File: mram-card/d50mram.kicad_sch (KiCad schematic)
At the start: 42 parts

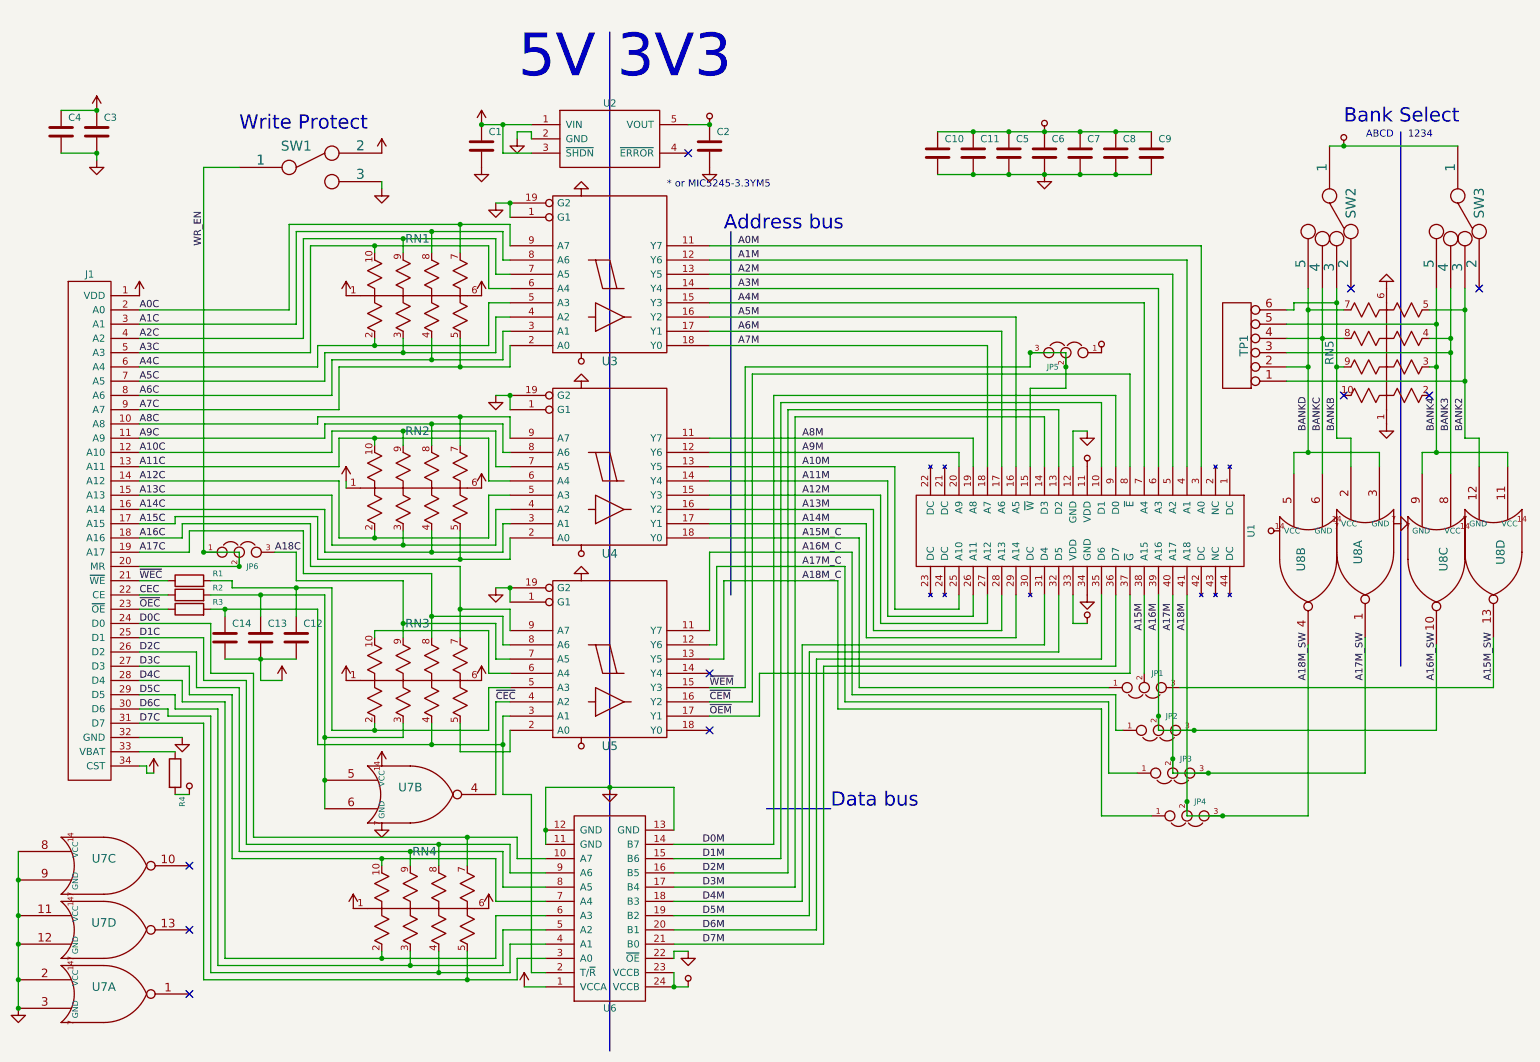
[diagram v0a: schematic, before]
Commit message: extracted the footprints from pcb file and reassigned the footprint mapping.
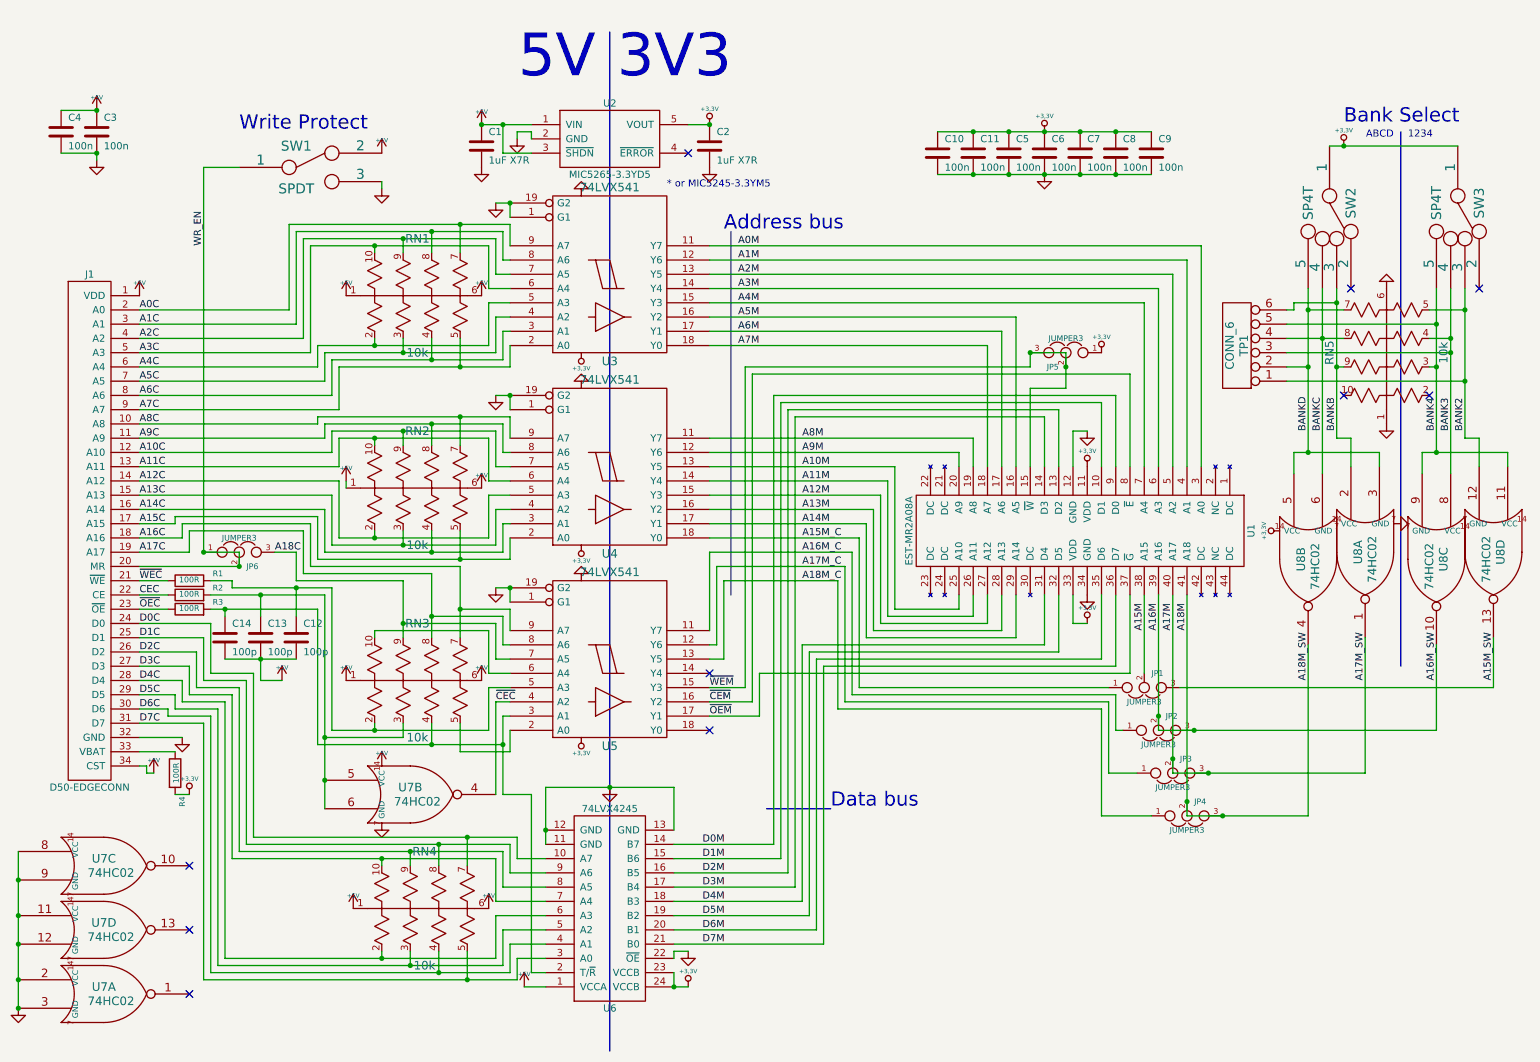
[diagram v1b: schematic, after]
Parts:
- C1, C2: value (none) -> 1uF X7R; footprint (none) -> Capacitor_SMD:C_0603_1608Metric
- C10, C11, C3, C4, C5, C6, C7, C8, C9: value (none) -> 100n; footprint (none) -> Capacitor_SMD:C_0603_1608Metric
- C12, C13, C14: value (none) -> 100p; footprint (none) -> Capacitor_SMD:C_0603_1608Metric
- J1: value (none) -> D50-EDGECONN; footprint (none) -> parts:EDGE1S34
- JP1, JP2, JP3, JP4, JP5, JP6: value (none) -> JUMPER3; footprint (none) -> parts:S_JUMPER_3
- R1, R2, R3, R4: value (none) -> 100R; footprint (none) -> Resistor_SMD:R_0603_1608Metric
- RN1, RN2, RN3, RN4, RN5: value (none) -> 10k; footprint (none) -> parts:CAT25
- SW1: value (none) -> SPDT; footprint (none) -> parts:CUS-12B
- SW2, SW3: value (none) -> SP4T; footprint (none) -> parts:CUS-14B
- TP1: value (none) -> CONN_6; footprint (none) -> parts:6P_TESTPT
- U1: value (none) -> EST-MR2A08A; footprint (none) -> parts:TSOP2-44
- U2: value (none) -> MIC5265-3.3YD5; footprint (none) -> parts:SOT23-5
- U3, U4, U5: value (none) -> 74LVX541; footprint (none) -> parts:tssop-20
- U6: value (none) -> 74LVX4245; footprint (none) -> parts:tssop-24
- U7, U8: value (none) -> 74HC02; footprint (none) -> parts:tssop-14
